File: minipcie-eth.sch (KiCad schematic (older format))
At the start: 7 parts

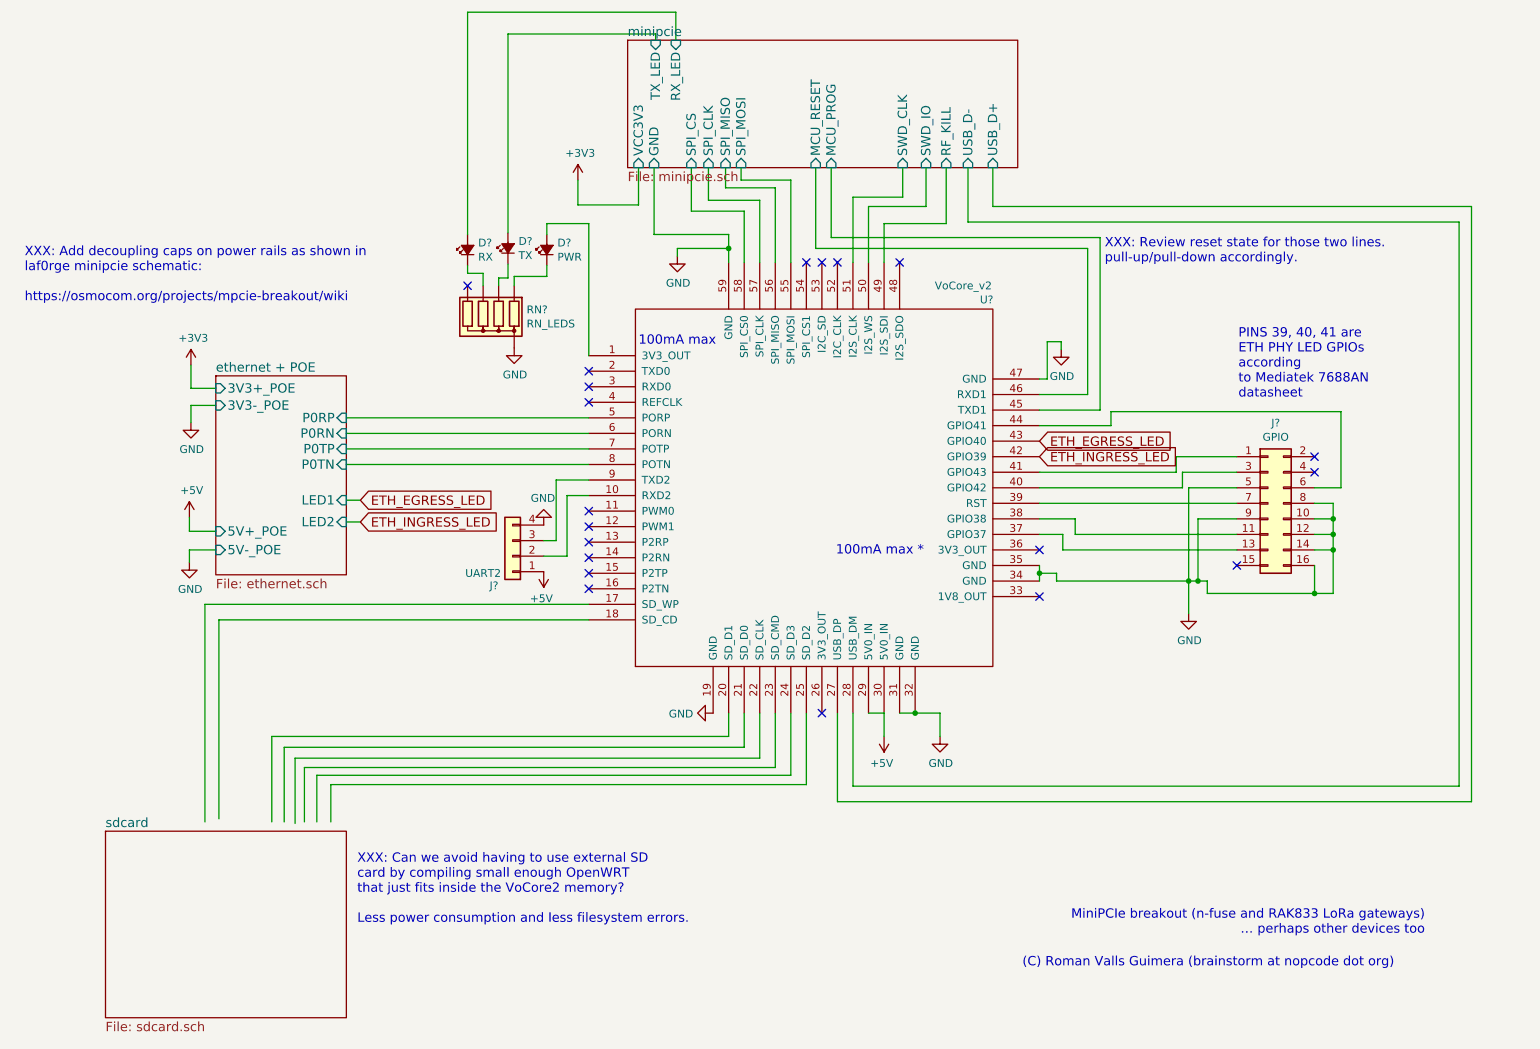
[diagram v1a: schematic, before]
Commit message: Added SDcard wiring
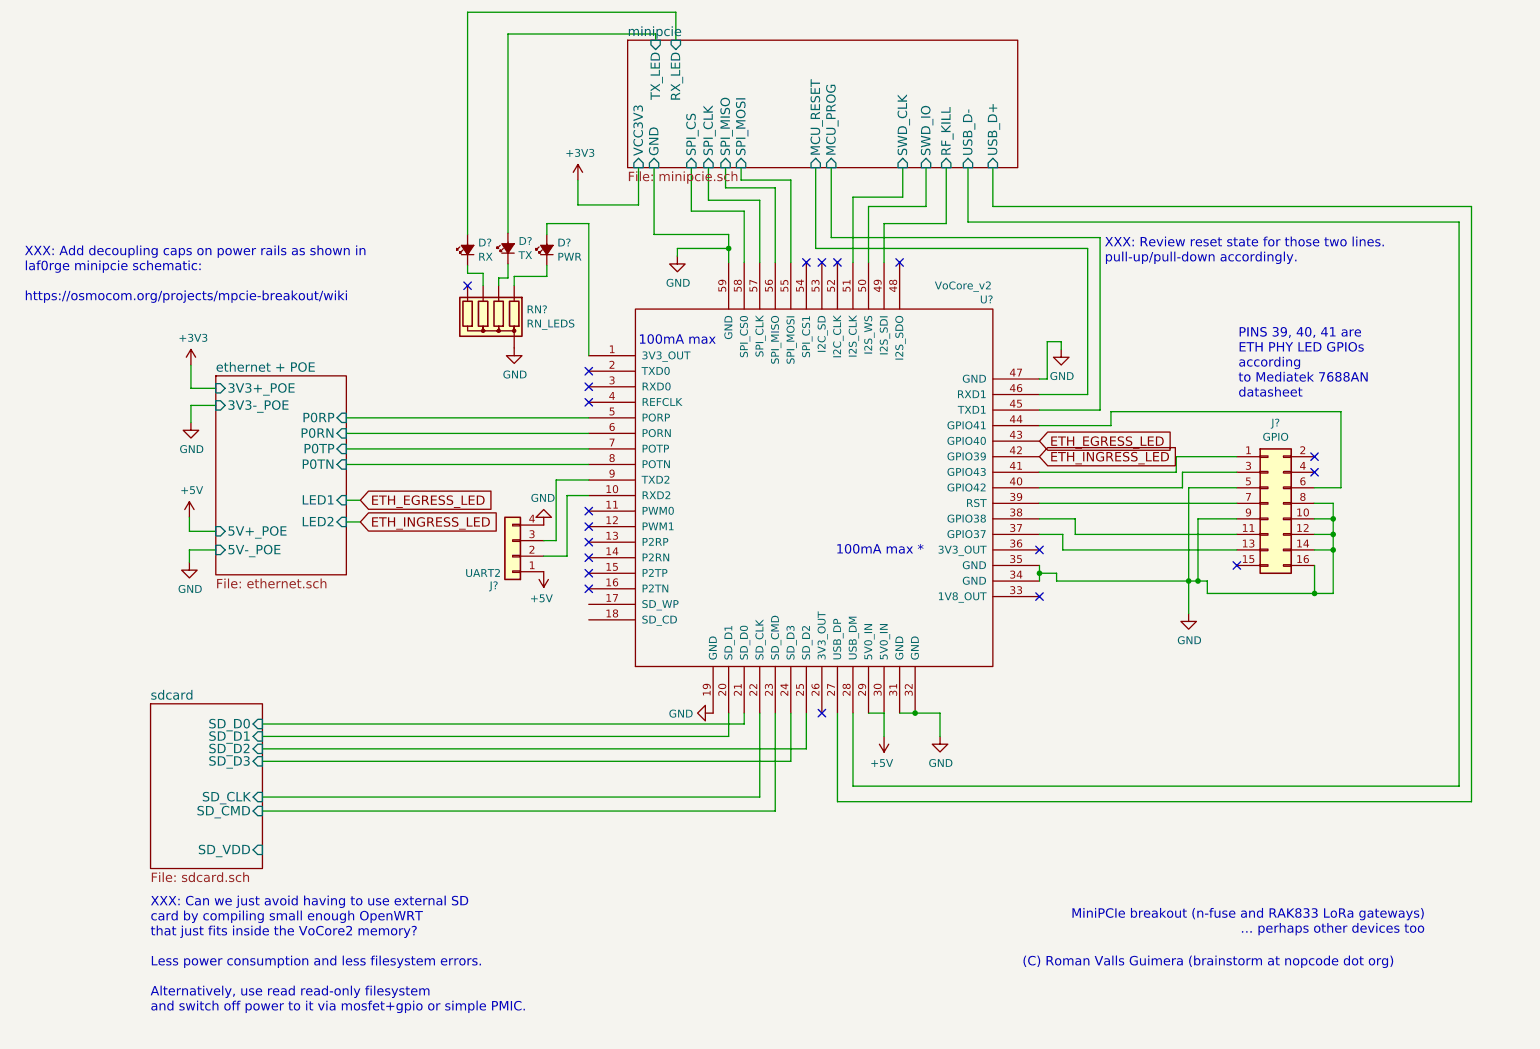
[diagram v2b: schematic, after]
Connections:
- wire segments 159 -> 149
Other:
- note added: "XXX: Can we just avoid having to use external SD \ncard by compiling small enough OpenWRT \nthat just fits inside the VoCore2 memory?\n\nLess power consumption and less filesystem errors.\n\nAlternatively, use read read-only filesystem \nand switch off power to it via mosfet+gpio or simple PMIC."
- note removed: "XXX: Can we avoid having to use external SD \ncard by compiling small enough OpenWRT \nthat just fits inside the VoCore2 memory?\n\nLess power consumption and less filesystem errors."
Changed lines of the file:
@@
-$EndSheet
-$Sheet
-S 1150 6140 1550 1200
-U 5BAF0F57
-F0 "sdcard" 60
-F1 "sdcard.sch" 60
 $EndSheet
 $Sheet
@@
 	8040 3830 7160 3830
 Wire Wire Line
-	8930 4330 9050 4330
+	9050 4330 8930 4330
 Wire Wire Line
 	9050 4610 9050 4330
@@
 	5860 5380 5860 5950
 Wire Wire Line
-	4260 4680 1790 4680
-Wire Wire Line
-	1790 4680 1790 6080
-Wire Wire Line
-	4260 4780 1880 4780
-Wire Wire Line
-	1880 4780 1880 6060
-Wire Wire Line
-	5660 5380 5660 5840
-Wire Wire Line
-	5660 5840 2600 5840
-Wire Wire Line
-	2600 5840 2600 6080
-Wire Wire Line
-	5560 5380 5560 5780
-Wire Wire Line
-	5560 5780 2510 5780
-Wire Wire Line
-	2510 5780 2510 6080
-Wire Wire Line
-	5460 5380 5460 5730
-Wire Wire Line
-	5460 5730 2430 5730
-Wire Wire Line
-	2430 5730 2430 6080
-Wire Wire Line
-	5360 5380 5360 5670
-Wire Wire Line
-	5360 5670 2370 5670
-Wire Wire Line
-	2370 5670 2370 6090
-Wire Wire Line
-	5260 5380 5260 5600
-Wire Wire Line
-	5260 5600 2300 5600
-Wire Wire Line
-	2300 5600 2300 6080
-Wire Wire Line
-	5160 5380 5160 5530
-Wire Wire Line
-	5160 5530 2220 5530
-Wire Wire Line
-	2220 5530 2220 6080
+	5660 5610 5660 5380
+Wire Wire Line
+	2160 5610 5660 5610
+Wire Wire Line
+	5560 5690 5560 5380
+Wire Wire Line
+	2160 5690 5560 5690
+Wire Wire Line
+	5460 6010 5460 5380
+Wire Wire Line
+	2160 6010 5460 6010
+Wire Wire Line
+	5360 5920 5360 5380
+Wire Wire Line
+	2160 5920 5360 5920
+Wire Wire Line
+	5260 5450 5260 5380
+Wire Wire Line
+	2160 5450 5260 5450
+Wire Wire Line
+	5160 5530 5160 5380
+Wire Wire Line
+	2160 5530 5160 5530
 Wire Wire Line
 	2700 3480 4260 3480
@@
 Wire Wire Line
 	6560 2230 6560 1870
-Text Notes 2770 6740 0    60   ~ 0
-XXX: Can we avoid having to use external SD \ncard by compiling small enough OpenWRT \nthat just fits inside the VoCore2 memory?\n\nLess power consumption and less filesystem errors.
+Text Notes 1440 7310 0    60   ~ 0
+XXX: Can we just avoid having to use external SD \ncard by compiling small enough OpenWRT \nthat just fits inside the VoCore2 memory?\n\nLess power consumption and less filesystem errors.\n\nAlternatively, use read read-only filesystem \nand switch off power to it via mosfet+gpio or simple PMIC.
 Text Notes 7580 2490 0    60   ~ 0
 XXX: Review reset state for those two lines.\npull-up/pull-down accordingly.
@@
 Text Notes 630  2740 0    60   ~ 0
 XXX: Add decoupling caps on power rails as shown in\nlaf0rge minipcie schematic:\n\nhttps://osmocom.org/projects/mpcie-breakout/wiki
+$Sheet
+S 1440 5320 720  1060
+U 5BAF0F57
+F0 "sdcard" 60
+F1 "sdcard.sch" 60
+F2 "SD_D0" I R 2160 5450 60
+F3 "SD_D1" I R 2160 5530 60
+F4 "SD_D2" I R 2160 5610 60
+F5 "SD_D3" I R 2160 5690 60
+F6 "SD_CMD" I R 2160 6010 60
+F7 "SD_CLK" I R 2160 5920 60
+F8 "SD_VDD" I R 2160 6260 60
+$EndSheet
 $EndSCHEMATC

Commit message: Rearrange components, validate package sizes, think about power plane placement since the ref design is 4 layers... can I add snubbers and other filtering and avoid 4-layer design?
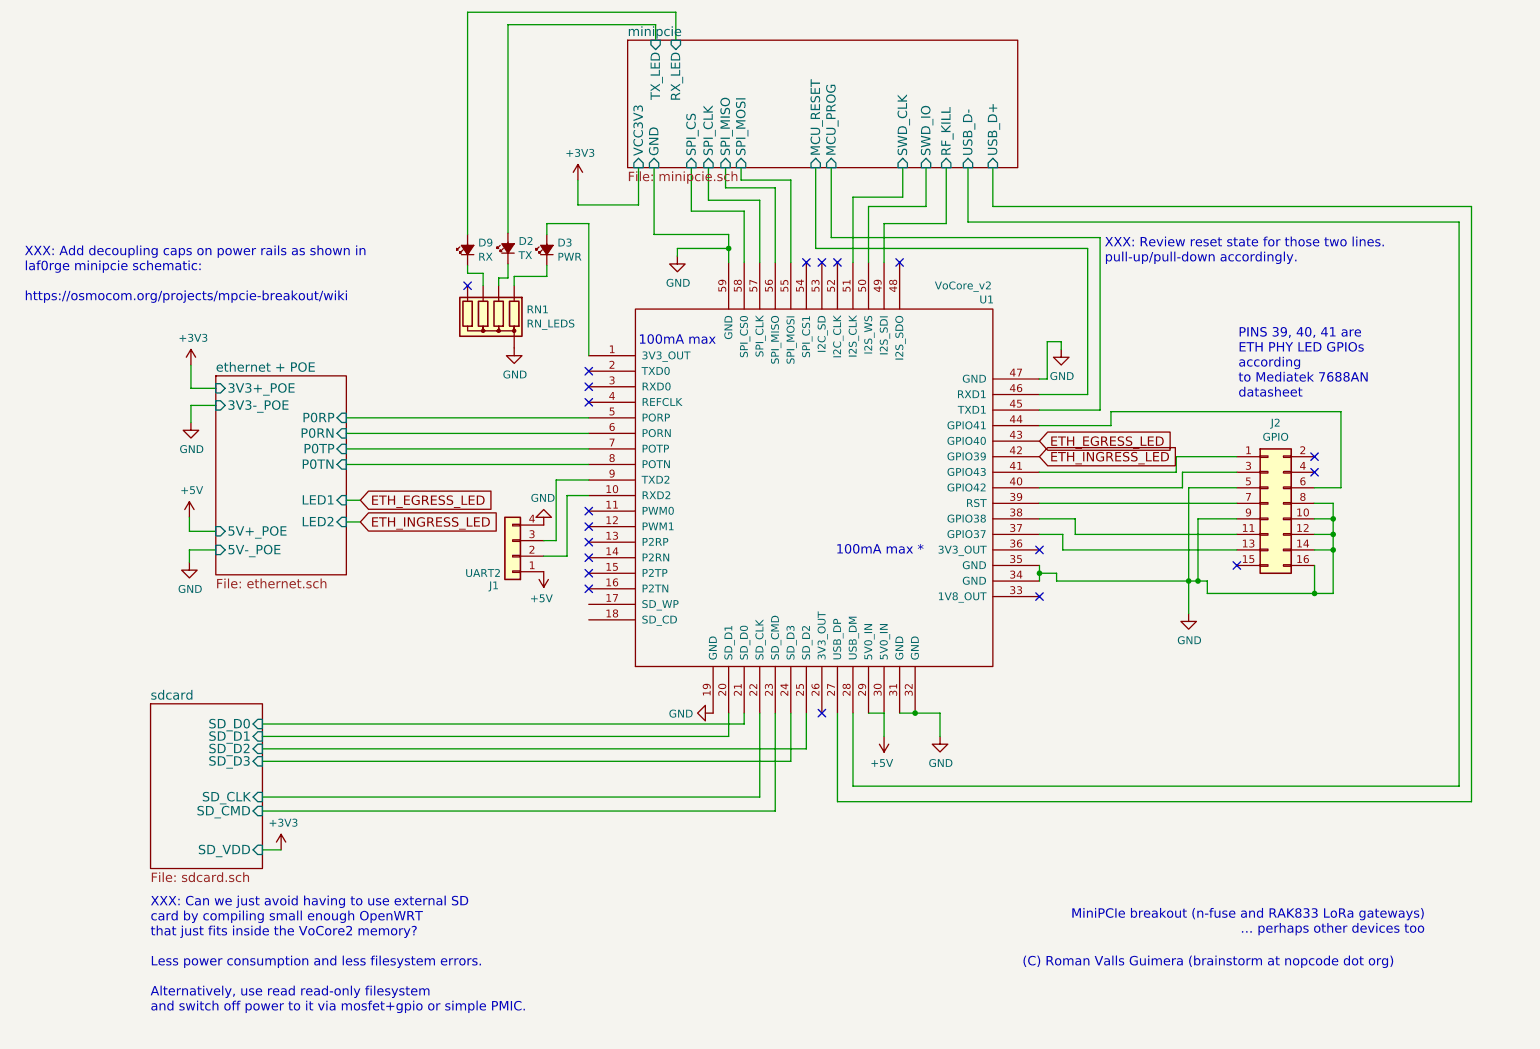
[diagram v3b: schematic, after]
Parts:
- D2, D3, D9: renamed from D?; footprint (none) -> KiCad/Diodes_SMD.pretty:D_0603
- J1: renamed from J?; footprint (none) -> KiCad/Pin_Headers.pretty:Pin_Header_Straight_1x04_Pitch2.54mm
- J2: renamed from J?; footprint (none) -> KiCad/Pin_Headers.pretty:Pin_Header_Straight_2x08_Pitch2.54mm
- RN1: renamed from RN?; footprint Resistors_THT:R_Array_SIP5 -> KiCad/Resistors_SMD.pretty:R_Array_Concave_4x0603
- U1: renamed from U?; footprint MODULE -> win:VoCore_v2
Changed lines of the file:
@@
 $EndDescr
 $Comp
-L VoCore_v2 U?
+L VoCore_v2 U1
 U 1 1 5BAF0D89
 P 5710 3930
-F 0 "U?" H 6820 5140 50  0000 C CNN
+F 0 "U1" H 6820 5140 50  0000 C CNN
 F 1 "VoCore_v2" H 6670 5230 50  0000 C CNN
-F 2 "MODULE" H 5710 3580 50  0001 C CNN
+F 2 "win:VoCore_v2" H 5710 3580 50  0001 C CNN
 F 3 "DOCUMENTATION" H 5710 3480 50  0001 C CNN
 	1    5710 3930
@@
 $EndSheet
 $Comp
-L Conn_01x04 J?
+L Conn_01x04 J1
 U 1 1 5BAF1493
 P 3770 4370
-F 0 "J?" H 3890 4560 50  0000 C CNN
+F 0 "J1" H 3890 4560 50  0000 C CNN
 F 1 "UART2" H 3960 4480 50  0000 C CNN
-F 2 "" H 3770 4370 50  0001 C CNN
+F 2 "KiCad/Pin_Headers.pretty:Pin_Header_Straight_1x04_Pitch2.54mm" H 3770 4370 50  0001 C CNN
 F 3 "" H 3770 4370 50  0001 C CNN
 	1    3770 4370
@@
 $EndComp
 $Comp
-L GND #PWR?
+L GND #PWR01
 U 1 1 5BAF1546
 P 6520 5530
-F 0 "#PWR?" H 6520 5280 50  0001 C CNN
+F 0 "#PWR01" H 6520 5280 50  0001 C CNN
 F 1 "GND" H 6525 5357 50  0000 C CNN
 F 2 "" H 6520 5530 50  0001 C CNN
@@
 $EndComp
 $Comp
-L GND #PWR?
+L GND #PWR02
 U 1 1 5BAF157A
 P 5060 5380
-F 0 "#PWR?" H 5060 5130 50  0001 C CNN
+F 0 "#PWR02" H 5060 5130 50  0001 C CNN
 F 1 "GND" V 5065 5252 50  0000 R CNN
 F 2 "" H 5060 5380 50  0001 C CNN
@@
 $EndComp
 $Comp
-L GND #PWR?
+L GND #PWR03
 U 1 1 5BAF158B
 P 8120 4740
-F 0 "#PWR?" H 8120 4490 50  0001 C CNN
+F 0 "#PWR03" H 8120 4490 50  0001 C CNN
 F 1 "GND" H 8125 4567 50  0000 C CNN
 F 2 "" H 8120 4740 50  0001 C CNN
@@
 $EndComp
 $Comp
-L GND #PWR?
+L GND #PWR04
 U 1 1 5BAF15B1
 P 4830 2440
-F 0 "#PWR?" H 4830 2190 50  0001 C CNN
+F 0 "#PWR04" H 4830 2190 50  0001 C CNN
 F 1 "GND" H 4835 2267 50  0000 C CNN
 F 2 "" H 4830 2440 50  0001 C CNN
@@
 $EndComp
 $Comp
-L +5V #PWR?
+L +5V #PWR05
 U 1 1 5BAF166D
 P 6160 5530
-F 0 "#PWR?" H 6160 5380 50  0001 C CNN
+F 0 "#PWR05" H 6160 5380 50  0001 C CNN
 F 1 "+5V" H 6175 5703 50  0000 C CNN
 F 2 "" H 6160 5530 50  0001 C CNN
@@
 NoConn ~ 7160 4630
 $Comp
-L Conn_02x08_Odd_Even J?
+L Conn_02x08_Odd_Even J2
 U 1 1 5BAF1E64
 P 8630 4030
-F 0 "J?" H 8680 4547 50  0000 C CNN
+F 0 "J2" H 8680 4547 50  0000 C CNN
 F 1 "GPIO" H 8680 4456 50  0000 C CNN
-F 2 "" H 8630 4030 50  0001 C CNN
+F 2 "KiCad/Pin_Headers.pretty:Pin_Header_Straight_2x08_Pitch2.54mm" H 8630 4030 50  0001 C CNN
 F 3 "" H 8630 4030 50  0001 C CNN
 	1    8630 4030
@@
 $EndComp
 $Comp
-L +5V #PWR?
+L +5V #PWR06
 U 1 1 5BAF2AC1
 P 3970 4470
-F 0 "#PWR?" H 3970 4320 50  0001 C CNN
+F 0 "#PWR06" H 3970 4320 50  0001 C CNN
 F 1 "+5V" H 3985 4643 50  0000 C CNN
 F 2 "" H 3970 4470 50  0001 C CNN
@@
 $EndComp
 $Comp
-L GND #PWR?
+L GND #PWR07
 U 1 1 5BAF2AD4
 P 3970 4170
-F 0 "#PWR?" H 3970 3920 50  0001 C CNN
+F 0 "#PWR07" H 3970 3920 50  0001 C CNN
 F 1 "GND" H 3975 3997 50  0000 C CNN
 F 2 "" H 3970 4170 50  0001 C CNN
@@
 	6160 5380 6160 5530
 Wire Wire Line
-	6260 5380 6360 5380
-Wire Wire Line
-	6360 5380 6520 5380
+	6260 5380 6520 5380
 Wire Wire Line
 	6520 5380 6520 5530
 Connection ~ 6360 5380
 Wire Wire Line
-	5160 2300 5160 2390
-Wire Wire Line
-	5160 2390 5160 2480
+	5160 2300 5160 2480
 Wire Wire Line
 	5160 2390 4830 2390
@@
 	4830 2390 4830 2440
 Wire Wire Line
-	7160 4430 7160 4480
-Wire Wire Line
-	7160 4480 7160 4530
-Wire Wire Line
-	7270 4530 8120 4530
-Wire Wire Line
-	8120 4530 8180 4530
-Wire Wire Line
-	8180 4530 8240 4530
+	7160 4430 7160 4530
+Wire Wire Line
+	7270 4530 8240 4530
 Wire Wire Line
 	8240 4530 8240 4610
 Wire Wire Line
-	8240 4610 8930 4610
-Wire Wire Line
-	8930 4610 9050 4610
+	8240 4610 9050 4610
 Wire Wire Line
 	8930 4610 8930 4430
@@
 	8430 3930 8120 3930
 Wire Wire Line
-	8120 3930 8120 4530
-Wire Wire Line
-	8120 4530 8120 4740
+	8120 3930 8120 4740
 Connection ~ 8120 4530
 Wire Wire Line
@@
 	9050 4330 8930 4330
 Wire Wire Line
-	9050 4610 9050 4330
-Wire Wire Line
-	9050 4330 9050 4230
-Wire Wire Line
-	9050 4230 9050 4130
-Wire Wire Line
-	9050 4130 9050 4030
+	9050 4610 9050 4030
 Connection ~ 8930 4610
 Wire Wire Line
@@
 XXX: Review reset state for those two lines.\npull-up/pull-down accordingly.
 $Comp
-L LED_Small_ALT D?
+L LED_Small_ALT D9
 U 1 1 5BB77A38
 P 3480 2400
-F 0 "D?" V 3526 2332 50  0000 R CNN
+F 0 "D9" V 3526 2332 50  0000 R CNN
 F 1 "RX" V 3435 2332 50  0000 R CNN
-F 2 "" V 3480 2400 50  0001 C CNN
+F 2 "KiCad/Diodes_SMD.pretty:D_0603" V 3480 2400 50  0001 C CNN
 F 3 "" V 3480 2400 50  0001 C CNN
 	1    3480 2400
@@
 $EndComp
 $Comp
-L LED_Small_ALT D?
+L LED_Small_ALT D2
 U 1 1 5BB77A74
 P 3740 2390
-F 0 "D?" V 3786 2322 50  0000 R CNN
+F 0 "D2" V 3786 2322 50  0000 R CNN
 F 1 "TX" V 3695 2322 50  0000 R CNN
-F 2 "" V 3740 2390 50  0001 C CNN
+F 2 "KiCad/Diodes_SMD.pretty:D_0603" V 3740 2390 50  0001 C CNN
 F 3 "" V 3740 2390 50  0001 C CNN
 	1    3740 2390
@@
 $EndComp
 $Comp
-L LED_Small_ALT D?
+L LED_Small_ALT D3
 U 1 1 5BB77AA6
 P 3990 2400
-F 0 "D?" V 4036 2332 50  0000 R CNN
+F 0 "D3" V 4036 2332 50  0000 R CNN
 F 1 "PWR" V 3945 2332 50  0000 R CNN
-F 2 "" V 3990 2400 50  0001 C CNN
+F 2 "KiCad/Diodes_SMD.pretty:D_0603" V 3990 2400 50  0001 C CNN
 F 3 "" V 3990 2400 50  0001 C CNN
 	1    3990 2400
@@
 $EndComp
 $Comp
-L R_Network04 RN?
+L R_Network04 RN1
 U 1 1 5BB77E7E
 P 3580 2830
-F 0 "RN?" H 3300 2784 50  0000 R CNN
+F 0 "RN1" H 3300 2784 50  0000 R CNN
 F 1 "RN_LEDS" H 3300 2875 50  0000 R CNN
-F 2 "Resistors_THT:R_Array_SIP5" V 3855 2830 50  0001 C CNN
+F 2 "KiCad/Resistors_SMD.pretty:R_Array_Concave_4x0603" V 3855 2830 50  0001 C CNN
 F 3 "" H 3580 2830 50  0001 C CNN
 	1    3580 2830
@@
 $EndComp
 $Comp
-L GND #PWR?
+L GND #PWR08
 U 1 1 5BB7822B
 P 3780 3030
-F 0 "#PWR?" H 3780 2780 50  0001 C CNN
+F 0 "#PWR08" H 3780 2780 50  0001 C CNN
 F 1 "GND" H 3785 2857 50  0000 C CNN
 F 2 "" H 3780 3030 50  0001 C CNN
@@
 	3990 2570 3990 2500
 Wire Wire Line
-	4690 1050 4690 1010
-Wire Wire Line
-	4690 1010 3740 1010
-Wire Wire Line
-	3740 1010 3740 2290
+	4690 1050 4690 950
+Wire Wire Line
+	4690 950  3740 950
+Wire Wire Line
+	3740 950  3740 2290
 Wire Wire Line
 	3740 2490 3740 2580
@@
 Connection ~ 7160 4480
 $Comp
-L GND #PWR?
+L GND #PWR09
 U 1 1 5BC0D564
 P 7300 3040
-F 0 "#PWR?" H 7300 2790 50  0001 C CNN
+F 0 "#PWR09" H 7300 2790 50  0001 C CNN
 F 1 "GND" H 7305 2867 50  0000 C CNN
 F 2 "" H 7300 3040 50  0001 C CNN
@@
 (C) Roman Valls Guimera (brainstorm at nopcode dot org)
 $Comp
-L GND #PWR?
+L GND #PWR010
 U 1 1 5BC3827A
 P 1690 4410
-F 0 "#PWR?" H 1690 4160 50  0001 C CNN
+F 0 "#PWR010" H 1690 4160 50  0001 C CNN
 F 1 "GND" H 1695 4237 50  0000 C CNN
 F 2 "" H 1690 4410 50  0001 C CNN
@@
 	1690 4210 1690 4120
 $Comp
-L +5V #PWR?
+L +5V #PWR011
 U 1 1 5BC389B7
 P 1690 4120
-F 0 "#PWR?" H 1690 3970 50  0001 C CNN
+F 0 "#PWR011" H 1690 3970 50  0001 C CNN
 F 1 "+5V" H 1705 4293 50  0000 C CNN
 F 2 "" H 1690 4120 50  0001 C CNN
@@
 $EndComp
 $Comp
-L GND #PWR?
+L GND #PWR012
 U 1 1 5BC444DB
 P 1700 3510
-F 0 "#PWR?" H 1700 3260 50  0001 C CNN
+F 0 "#PWR012" H 1700 3260 50  0001 C CNN
 F 1 "GND" H 1705 3337 50  0000 C CNN
 F 2 "" H 1700 3510 50  0001 C CNN
@@
 ETH_INGRESS_LED
 $Comp
-L +3V3 #PWR?
+L +3V3 #PWR013
 U 1 1 5BC46C2B
 P 1700 3140
-F 0 "#PWR?" H 1700 2990 50  0001 C CNN
+F 0 "#PWR013" H 1700 2990 50  0001 C CNN
 F 1 "+3V3" H 1715 3313 50  0000 C CNN
 F 2 "" H 1700 3140 50  0001 C CNN
@@
 $EndComp
 $Comp
-L +3V3 #PWR?
+L +3V3 #PWR014
 U 1 1 5BC46E95
 P 4190 1950
-F 0 "#PWR?" H 4190 1800 50  0001 C CNN
+F 0 "#PWR014" H 4190 1800 50  0001 C CNN
 F 1 "+3V3" H 4205 2123 50  0000 C CNN
 F 2 "" H 4190 1950 50  0001 C CNN
@@
 F8 "SD_VDD" I R 2160 6260 60
 $EndSheet
+$Comp
+L +3V3 #PWR015
+U 1 1 5BC5E4DC
+P 2280 6260
+F 0 "#PWR015" H 2280 6110 50  0001 C CNN
+F 1 "+3V3" H 2295 6433 50  0000 C CNN
+F 2 "" H 2280 6260 50  0001 C CNN
+F 3 "" H 2280 6260 50  0001 C CNN
+	1    2280 6260
+	1    0    0    -1
+$EndComp
+Wire Wire Line
+	2160 6260 2280 6260
 $EndSCHEMATC
